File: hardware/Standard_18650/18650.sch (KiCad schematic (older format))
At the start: 56 parts, among them J2 Battery, J3 GPIO, J4 USB_B_Micro, J5 Power, J6 LEDs, J7 GPIO, Q1 BSS806N, Q2 BSS806N, Q3 BSS806N, Q4 BSS806N, SW1 Mode, SW2 Power, U1 STM32F412CGUx, U2 AP2210N-3.3TRG1, U3 BQ21040, U4 ESD7002WTT1G, Y1 32.768kHz

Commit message: Update gerbers for pcbway
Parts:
- C11, C13, C2, C6: value 1uf -> 1uF
- C15, C16, C3, C4, C5: value 100nf -> 100nF
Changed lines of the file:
@@
 P 6200 1400
 F 0 "C3" H 6300 1400 50  0000 L CNN
-F 1 "100nf" H 6200 1300 50  0000 L CNN
+F 1 "100nF" H 6200 1300 50  0000 L CNN
 F 2 "Capacitor_SMD:C_0603_1608Metric" H 6200 1400 50  0001 C CNN
 F 3 "~" H 6200 1400 50  0001 C CNN
@@
 P 5950 1400
 F 0 "C2" H 5750 1400 50  0000 L CNN
-F 1 "1uf" H 5950 1300 50  0000 L CNN
+F 1 "1uF" H 5950 1300 50  0000 L CNN
 F 2 "Capacitor_SMD:C_0603_1608Metric" H 5950 1400 50  0001 C CNN
 F 3 "~" H 5950 1400 50  0001 C CNN
@@
 P 4400 1450
 F 0 "C4" H 4450 1450 50  0000 L CNN
-F 1 "100nf" H 4400 1350 50  0000 L CNN
+F 1 "100nF" H 4400 1350 50  0000 L CNN
 F 2 "Capacitor_SMD:C_0603_1608Metric" H 4400 1450 50  0001 C CNN
 F 3 "~" H 4400 1450 50  0001 C CNN
@@
 P 4650 1450
 F 0 "C5" H 4700 1450 50  0000 L CNN
-F 1 "100nf" H 4650 1350 50  0000 L CNN
+F 1 "100nF" H 4650 1350 50  0000 L CNN
 F 2 "Capacitor_SMD:C_0603_1608Metric" H 4650 1450 50  0001 C CNN
 F 3 "~" H 4650 1450 50  0001 C CNN
@@
 P 5350 7100
 F 0 "C6" H 5400 7000 50  0000 L CNN
-F 1 "1uf" H 5400 7200 50  0000 L CNN
+F 1 "1uF" H 5400 7200 50  0000 L CNN
 F 2 "Capacitor_SMD:C_0603_1608Metric" H 5388 6950 50  0001 C CNN
 F 3 "~" H 5350 7100 50  0001 C CNN
@@
 Wire Notes Line
 	2500 6350 2500 7700
-$Comp
-L Device:C C13
-U 1 1 5DAA61BD
-P 3450 7200
-F 0 "C13" H 3500 7100 50  0000 L CNN
-F 1 "1uf" H 3250 7300 50  0000 L CNN
-F 2 "Capacitor_SMD:C_0603_1608Metric" H 3488 7050 50  0001 C CNN
-F 3 "~" H 3450 7200 50  0001 C CNN
-F 4 "0603" H 3450 7200 50  0001 C CNN "Package"
-	1    3450 7200
-	1    0    0    1
-$EndComp
 Wire Wire Line
 	3300 6650 3450 6650
@@
 AR Path="/5DBF7250" Ref="C11"  Part="1"
 F 0 "C11" H 9875 5400 50  0000 L CNN
-F 1 "1uf" H 9875 5200 50  0000 L CNN
+F 1 "1uF" H 9875 5200 50  0000 L CNN
 F 2 "Capacitor_SMD:C_0603_1608Metric" H 9888 5150 50  0001 C CNN
 F 3 "" H 9850 5300 50  0001 C CNN
@@
 P 3850 1450
 F 0 "C15" H 3900 1450 50  0000 L CNN
-F 1 "100nf" H 3850 1350 50  0000 L CNN
+F 1 "100nF" H 3850 1350 50  0000 L CNN
 F 2 "Capacitor_SMD:C_0603_1608Metric" H 3850 1450 50  0001 C CNN
 F 3 "~" H 3850 1450 50  0001 C CNN
@@
 P 4100 1450
 F 0 "C16" H 4150 1450 50  0000 L CNN
-F 1 "100nf" H 4100 1350 50  0000 L CNN
+F 1 "100nF" H 4100 1350 50  0000 L CNN
 F 2 "Capacitor_SMD:C_0603_1608Metric" H 4100 1450 50  0001 C CNN
 F 3 "~" H 4100 1450 50  0001 C CNN
@@
 	1    0    0    -1
 $EndComp
+$Comp
+L Device:C C13
+U 1 1 5DAA61BD
+P 3450 7200
+F 0 "C13" H 3500 7100 50  0000 L CNN
+F 1 "1uF" H 3300 7300 50  0000 L CNN
+F 2 "Capacitor_SMD:C_0603_1608Metric" H 3488 7050 50  0001 C CNN
+F 3 "~" H 3450 7200 50  0001 C CNN
+F 4 "0603" H 3450 7200 50  0001 C CNN "Package"
+	1    3450 7200
+	1    0    0    1
+$EndComp
 $EndSCHEMATC

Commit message: Add HSE crystal
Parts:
- removed Y1: 32.768kHz, Crystal:Crystal_SMD_3215-2Pin_3.2x1.5mm, symbol Device:Crystal_Small
- added Y1: 24Mhz, Crystal:Crystal_SMD_2016-4Pin_2.0x1.6mm, symbol Device:Crystal_GND2_Small
- C10, C8: value 7pF -> 6pF; Digikey (none) -> 1276-2133-1-ND; MPN CL10C070CB8NNNC -> CL10C060CB8NNNC
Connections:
- wire segments 220 -> 223
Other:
- note added: "Oscillator"
- note removed: "Optional RTC Source"
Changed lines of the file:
@@
 XTAL1
 Text Notes 9100 3800 0    50   ~ 0
-Optional RTC Source
+Oscillator
 Wire Notes Line
 	9100 3800 9100 4400
@@
 P 9450 4200
 F 0 "C10" V 9500 4250 50  0000 L CNN
-F 1 "7pF" V 9550 4100 50  0000 L CNN
+F 1 "6pF" V 9550 4100 50  0000 L CNN
 F 2 "Capacitor_SMD:C_0603_1608Metric" H 9450 4200 50  0001 C CNN
 F 3 "~" H 9450 4200 50  0001 C CNN
-F 4 "CL10C070CB8NNNC" H 9450 4200 50  0001 C CNN "MPN"
+F 4 "CL10C060CB8NNNC" H 9450 4200 50  0001 C CNN "MPN"
 F 5 "0603" H 7200 1550 50  0001 C CNN "Package"
+F 6 "1276-2133-1-ND" H 9450 4200 50  0001 C CNN "Digikey"
 	1    9450 4200
 	0    1    1    0
 $EndComp
-$Comp
-L Device:Crystal_Small Y1
-U 1 1 5D480A74
-P 9750 4100
-F 0 "Y1" V 9750 3950 50  0000 C CNN
-F 1 "32.768kHz" V 9750 4400 50  0000 C CNN
-F 2 "Crystal:Crystal_SMD_3215-2Pin_3.2x1.5mm" H 9750 4100 50  0001 C CNN
-F 3 "~" H 9750 4100 50  0001 C CNN
-F 4 "FC-135 32.768KA-AG0" H 9750 4100 50  0001 C CNN "MPN"
-F 5 "SER4089CT-ND" H 9750 4100 50  0001 C CNN "Digikey"
-	1    9750 4100
-	0    1    1    0
-$EndComp
 Wire Wire Line
 	10050 4150 10050 4200
-Wire Wire Line
-	9750 4000 10050 4000
-Wire Wire Line
-	9550 4000 9750 4000
-Connection ~ 9750 4000
-Wire Wire Line
-	9750 4200 10050 4200
-Wire Wire Line
-	9750 4200 9550 4200
-Connection ~ 9750 4200
 $Comp
 L Device:C_Small C8
@@
 P 9450 4000
 F 0 "C8" V 9350 4050 50  0000 L CNN
-F 1 "7pF" V 9350 3900 50  0000 L CNN
+F 1 "6pF" V 9350 3900 50  0000 L CNN
 F 2 "Capacitor_SMD:C_0603_1608Metric" H 9450 4000 50  0001 C CNN
 F 3 "~" H 9450 4000 50  0001 C CNN
-F 4 "CL10C070CB8NNNC" H 9450 4000 50  0001 C CNN "MPN"
+F 4 "CL10C060CB8NNNC" H 9450 4000 50  0001 C CNN "MPN"
 F 5 "0603" H 7200 1550 50  0001 C CNN "Package"
+F 6 "1276-2133-1-ND" H 9450 4000 50  0001 C CNN "Digikey"
 	1    9450 4000
 	0    1    1    0
@@
 Wire Notes Line
 	9100 4400 10550 4400
-Text Label 2750 3150 2    50   ~ 0
+Text Label 2750 2750 2    50   ~ 0
 XTAL2
-Text Label 2750 3050 2    50   ~ 0
+Text Label 2750 2650 2    50   ~ 0
 XTAL1
 Wire Wire Line
@@
 NoConn ~ 2750 4750
 NoConn ~ 4050 4750
-NoConn ~ 2750 2650
-NoConn ~ 2750 2750
 NoConn ~ 2750 3350
 NoConn ~ 2750 3450
-NoConn ~ 2750 3550
 NoConn ~ 2750 3650
+Wire Wire Line
+	3350 1350 3450 1350
+Connection ~ 3350 1350
+Connection ~ 3450 1350
+Wire Wire Line
+	3450 1350 3550 1350
+Connection ~ 3550 1350
+Connection ~ 4650 1350
+Wire Wire Line
+	4650 1350 4900 1350
+Connection ~ 4750 1600
+Wire Wire Line
+	4650 1550 4650 1600
+Connection ~ 4650 1600
+Wire Wire Line
+	4650 1600 4750 1600
+Text Label 3650 1750 0    50   ~ 0
+VDDA
+$Comp
+L Device:C_Small C16
+U 1 1 5E4C3105
+P 4100 1450
+F 0 "C16" H 4150 1450 50  0000 L CNN
+F 1 "100nF" H 4100 1350 50  0000 L CNN
+F 2 "Capacitor_SMD:C_0603_1608Metric" H 4100 1450 50  0001 C CNN
+F 3 "~" H 4100 1450 50  0001 C CNN
+F 4 "AVX" H 4100 1450 50  0001 C CNN "MFN"
+F 5 "06035C104K4T2A" H 4100 1450 50  0001 C CNN "MPN"
+F 6 "0603" H -550 -250 50  0001 C CNN "Package"
+	1    4100 1450
+	1    0    0    -1
+$EndComp
+Connection ~ 3850 1350
+Wire Wire Line
+	3550 1350 3850 1350
+Wire Wire Line
+	3650 1850 3650 1750
+Wire Wire Line
+	3850 1350 4100 1350
+Connection ~ 4100 1350
+Wire Wire Line
+	3850 1550 3850 1600
+Wire Wire Line
+	3850 1600 4100 1600
+Wire Wire Line
+	4100 1550 4100 1600
+Connection ~ 4100 1600
+Connection ~ 4400 1350
+Wire Wire Line
+	4400 1350 4650 1350
+Wire Wire Line
+	4100 1350 4400 1350
+Wire Wire Line
+	4100 1600 4400 1600
+Wire Wire Line
+	4400 1550 4400 1600
+Connection ~ 4400 1600
+Wire Wire Line
+	4400 1600 4650 1600
+$Comp
+L Device:C_Small C14
+U 1 1 5E571D7C
+P 2350 2600
+F 0 "C14" H 2150 2650 50  0000 L CNN
+F 1 "4.7uF" H 2100 2500 50  0000 L CNN
+F 2 "Capacitor_SMD:C_0603_1608Metric" H 2350 2600 50  0001 C CNN
+F 3 "~" H 2350 2600 50  0001 C CNN
+F 4 "CL10A475KO8NNNC‎" H 2350 2600 50  0001 C CNN "MPN"
+F 5 "0603" H 2350 2600 50  0001 C CNN "Package"
+	1    2350 2600
+	1    0    0    -1
+$EndComp
+Wire Wire Line
+	2750 2450 2350 2450
+Wire Wire Line
+	2350 2450 2350 2500
+$Comp
+L power:GND #PWR0111
+U 1 1 5E581A13
+P 2350 2700
+F 0 "#PWR0111" H 2350 2450 50  0001 C CNN
+F 1 "GND" H 2355 2527 50  0000 C CNN
+F 2 "" H 2350 2700 50  0001 C CNN
+F 3 "" H 2350 2700 50  0001 C CNN
+	1    2350 2700
+	1    0    0    -1
+$EndComp
+$Comp
+L Device:C C13
+U 1 1 5DAA61BD
+P 3450 7200
+F 0 "C13" H 3500 7100 50  0000 L CNN
+F 1 "1uF" H 3300 7300 50  0000 L CNN
+F 2 "Capacitor_SMD:C_0603_1608Metric" H 3488 7050 50  0001 C CNN
+F 3 "~" H 3450 7200 50  0001 C CNN
+F 4 "0603" H 3450 7200 50  0001 C CNN "Package"
+	1    3450 7200
+	1    0    0    1
+$EndComp
+Wire Wire Line
+	3550 1850 3550 1350
+Wire Wire Line
+	3450 1350 3450 1850
 Wire Wire Line
 	3350 1350 3350 1850
@@
 	1    0    0    -1
 $EndComp
-Wire Wire Line
-	3350 1350 3450 1350
-Connection ~ 3350 1350
-Wire Wire Line
-	3450 1350 3450 1850
-Connection ~ 3450 1350
-Wire Wire Line
-	3450 1350 3550 1350
-Wire Wire Line
-	3550 1850 3550 1350
-Connection ~ 3550 1350
-Connection ~ 4650 1350
-Wire Wire Line
-	4650 1350 4900 1350
-Connection ~ 4750 1600
-Wire Wire Line
-	4650 1550 4650 1600
-Connection ~ 4650 1600
-Wire Wire Line
-	4650 1600 4750 1600
-Text Label 3650 1750 0    50   ~ 0
-VDDA
+NoConn ~ 2750 2950
+$Comp
+L power:GND #PWR0112
+U 1 1 5E48991B
+P 2150 3650
+F 0 "#PWR0112" H 2150 3400 50  0001 C CNN
+F 1 "GND" H 2155 3477 50  0000 C CNN
+F 2 "" H 2150 3650 50  0001 C CNN
+F 3 "" H 2150 3650 50  0001 C CNN
+	1    2150 3650
+	1    0    0    -1
+$EndComp
+Wire Wire Line
+	2150 3650 2150 3550
+Wire Wire Line
+	2150 3550 2750 3550
+NoConn ~ 2750 3050
+NoConn ~ 2750 3150
+$Comp
+L Device:Crystal_GND2_Small Y1
+U 1 1 5E4E60E4
+P 9800 4100
+F 0 "Y1" V 9600 4050 50  0000 L CNN
+F 1 "24Mhz" V 9800 4200 50  0000 L CNN
+F 2 "Crystal:Crystal_SMD_2016-4Pin_2.0x1.6mm" H 9800 4100 50  0001 C CNN
+F 3 "~" H 9800 4100 50  0001 C CNN
+F 4 "XRCGB24M000F0L00R0" H 9800 4100 50  0001 C CNN "MPN"
+F 5 "490-5575-1-ND" H 9800 4100 50  0001 C CNN "Digikey"
+F 6 "4-SMD" V 9891 4188 50  0001 L CNN "Package"
+	1    9800 4100
+	0    1    1    0
+$EndComp
+Wire Wire Line
+	9550 4000 9800 4000
+Wire Wire Line
+	9550 4200 9800 4200
+Connection ~ 9800 4000
+Wire Wire Line
+	9800 4000 10050 4000
+Connection ~ 9800 4200
+Wire Wire Line
+	9800 4200 10050 4200
+Wire Wire Line
+	9700 4100 9300 4100
 $Comp
 L Device:C_Small C15
@@
 	1    0    0    -1
 $EndComp
-$Comp
-L Device:C_Small C16
-U 1 1 5E4C3105
-P 4100 1450
-F 0 "C16" H 4150 1450 50  0000 L CNN
-F 1 "100nF" H 4100 1350 50  0000 L CNN
-F 2 "Capacitor_SMD:C_0603_1608Metric" H 4100 1450 50  0001 C CNN
-F 3 "~" H 4100 1450 50  0001 C CNN
-F 4 "AVX" H 4100 1450 50  0001 C CNN "MFN"
-F 5 "06035C104K4T2A" H 4100 1450 50  0001 C CNN "MPN"
-F 6 "0603" H -550 -250 50  0001 C CNN "Package"
-	1    4100 1450
-	1    0    0    -1
-$EndComp
-Connection ~ 3850 1350
-Wire Wire Line
-	3550 1350 3850 1350
-Wire Wire Line
-	3650 1850 3650 1750
-Wire Wire Line
-	3850 1350 4100 1350
-Connection ~ 4100 1350
-Wire Wire Line
-	3850 1550 3850 1600
-Wire Wire Line
-	3850 1600 4100 1600
-Wire Wire Line
-	4100 1550 4100 1600
-Connection ~ 4100 1600
-Connection ~ 4400 1350
-Wire Wire Line
-	4400 1350 4650 1350
-Wire Wire Line
-	4100 1350 4400 1350
-Wire Wire Line
-	4100 1600 4400 1600
-Wire Wire Line
-	4400 1550 4400 1600
-Connection ~ 4400 1600
-Wire Wire Line
-	4400 1600 4650 1600
-$Comp
-L Device:C_Small C14
-U 1 1 5E571D7C
-P 2350 2600
-F 0 "C14" H 2150 2650 50  0000 L CNN
-F 1 "4.7uF" H 2100 2500 50  0000 L CNN
-F 2 "Capacitor_SMD:C_0603_1608Metric" H 2350 2600 50  0001 C CNN
-F 3 "~" H 2350 2600 50  0001 C CNN
-F 4 "CL10A475KO8NNNC‎" H 2350 2600 50  0001 C CNN "MPN"
-F 5 "0603" H 2350 2600 50  0001 C CNN "Package"
-	1    2350 2600
-	1    0    0    -1
-$EndComp
-Wire Wire Line
-	2750 2450 2350 2450
-Wire Wire Line
-	2350 2450 2350 2500
-$Comp
-L power:GND #PWR0111
-U 1 1 5E581A13
-P 2350 2700
-F 0 "#PWR0111" H 2350 2450 50  0001 C CNN
-F 1 "GND" H 2355 2527 50  0000 C CNN
-F 2 "" H 2350 2700 50  0001 C CNN
-F 3 "" H 2350 2700 50  0001 C CNN
-	1    2350 2700
-	1    0    0    -1
-$EndComp
-$Comp
-L Device:C C13
-U 1 1 5DAA61BD
-P 3450 7200
-F 0 "C13" H 3500 7100 50  0000 L CNN
-F 1 "1uF" H 3300 7300 50  0000 L CNN
-F 2 "Capacitor_SMD:C_0603_1608Metric" H 3488 7050 50  0001 C CNN
-F 3 "~" H 3450 7200 50  0001 C CNN
-F 4 "0603" H 3450 7200 50  0001 C CNN "Package"
-	1    3450 7200
-	1    0    0    1
-$EndComp
 $EndSCHEMATC

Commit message: Add extra ground pin.
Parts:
- C12: MPN (none) -> CL10A225KO8NNNC
- J5: footprint Connector_PinHeader_2.54mm:PinHeader_1x04_P2.54mm_Vertical -> Connector_PinHeader_2.54mm:PinHeader_1x05_P2.54mm_Vertical; symbol Connector_Generic:Conn_01x04 -> Connector_Generic:Conn_01x05
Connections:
- net +3V3: now also J5.4 (Pin_4); no longer J5.3 (Pin_3)
- net GND: now also J5.2 (Pin_2)
- net VIN: now also J5.5 (Pin_5); no longer J5.4 (Pin_4)
- net VUSB: now also J5.3 (Pin_3); no longer J5.2 (Pin_2)
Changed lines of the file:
@@
 L power:GND #PWR0129
 U 1 1 5C2D8F0C
-P 2550 5650
-F 0 "#PWR0129" H 2550 5400 50  0001 C CNN
-F 1 "GND" H 2555 5477 50  0000 C CNN
-F 2 "" H 2550 5650 50  0001 C CNN
-F 3 "" H 2550 5650 50  0001 C CNN
-	1    2550 5650
-	1    0    0    -1
-$EndComp
-$Comp
-L Connector_Generic:Conn_01x04 J?
+P 2650 5800
+F 0 "#PWR0129" H 2650 5550 50  0001 C CNN
+F 1 "GND" H 2655 5627 50  0000 C CNN
+F 2 "" H 2650 5800 50  0001 C CNN
+F 3 "" H 2650 5800 50  0001 C CNN
+	1    2650 5800
+	1    0    0    -1
+$EndComp
+$Comp
+L Connector_Generic:Conn_01x05 J?
 U 1 1 5C2B93C1
 P 2350 5550
@@
 F 0 "J5" H 2429 5542 50  0000 L CNN
 F 1 "Power" H 2429 5451 50  0000 L CNN
-F 2 "Connector_PinHeader_2.54mm:PinHeader_1x04_P2.54mm_Vertical" H 2350 5550 50  0001 C CNN
+F 2 "Connector_PinHeader_2.54mm:PinHeader_1x05_P2.54mm_Vertical" H 2350 5550 50  0001 C CNN
 F 3 "~" H 2350 5550 50  0001 C CNN
 	1    2350 5550
@@
 F 1 "2.2uF" H 6550 7200 50  0000 L CNN
 F 2 "Capacitor_SMD:C_0603_1608Metric" H 6488 6950 50  0001 C CNN
-F 3 "~" H 6450 7100 50  0001 C CNN
+F 3 "" H 6450 7100 50  0001 C CNN
 F 4 "0603" H 6450 7100 50  0001 C CNN "Package"
+F 5 "CL10A225KO8NNNC" H 6450 7100 50  0001 C CNN "MPN"
 	1    6450 7100
 	1    0    0    -1
@@
 	1    0    0    -1
 $EndComp
+Wire Wire Line
+	2550 5750 2650 5750
+Wire Wire Line
+	2650 5750 2650 5800
+Wire Wire Line
+	2550 5650 2650 5650
+Wire Wire Line
+	2650 5650 2650 5750
+Connection ~ 2650 5750
 $EndSCHEMATC

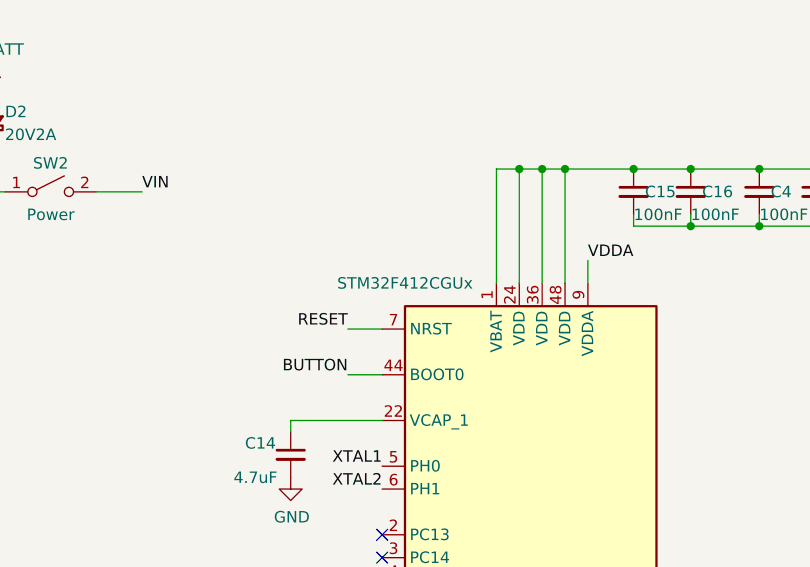
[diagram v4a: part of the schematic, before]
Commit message: Update pins and arduino examples.
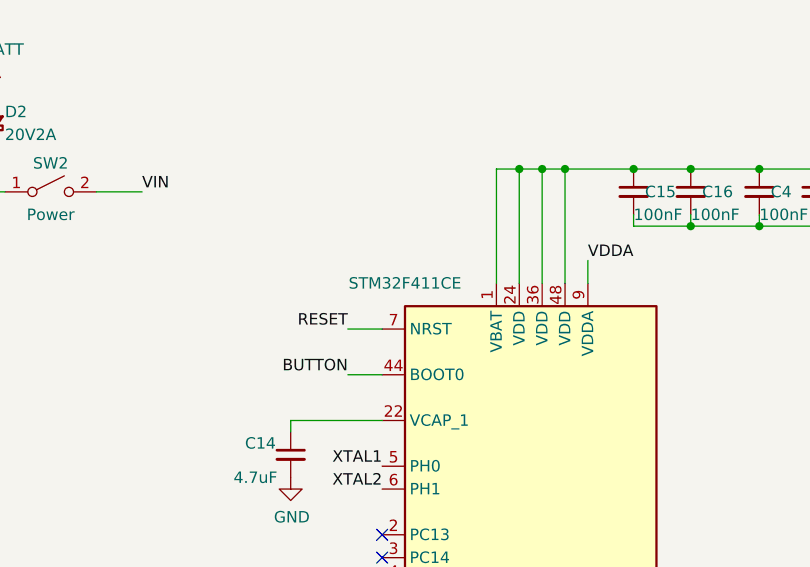
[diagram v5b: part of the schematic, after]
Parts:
- U1: value STM32F412CGUx -> STM32F411CE; MPN (none) -> STM32F411CE
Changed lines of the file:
@@
 P 3450 3350
 F 0 "U1" H 3850 1750 50  0000 C CNN
-F 1 "STM32F412CGUx" H 2850 4850 50  0000 C CNN
+F 1 "STM32F411CE" H 2850 4850 50  0000 C CNN
 F 2 "Package_DFN_QFN:QFN-48-1EP_7x7mm_P0.5mm_EP5.6x5.6mm" H 2850 1850 50  0001 R CNN
 F 3 "http://www.st.com/st-web-ui/static/active/en/resource/technical/document/datasheet/DM00213872.pdf" H 3450 3350 50  0001 C CNN
+F 4 "STM32F411CE" H 3450 3350 50  0001 C CNN "MPN"
 	1    3450 3350
 	1    0    0    -1

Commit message: Production boards.
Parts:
- R2: value 20K -> 20k
- R6: value 675 -> 680
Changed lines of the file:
@@
 AR Path="/5BE2C852" Ref="R2"  Part="1"
 F 0 "R2" V 1430 7200 50  0000 C CNN
-F 1 "20K" V 1350 7200 50  0000 C CNN
+F 1 "20k" V 1350 7200 50  0000 C CNN
 F 2 "Resistor_SMD:R_0603_1608Metric" V 1280 7200 50  0001 C CNN
 F 3 "" H 1350 7200 50  0001 C CNN
@@
 AR Path="/5DD411B8" Ref="R6"  Part="1"
 F 0 "R6" H 8300 5350 50  0000 L CNN
-F 1 "675" H 8300 5250 50  0000 L CNN
+F 1 "680" H 8300 5250 50  0000 L CNN
 F 2 "Resistor_SMD:R_0603_1608Metric" H 8250 5300 50  0001 C CNN
 F 3 "" H 8250 5300 50  0001 C CNN
